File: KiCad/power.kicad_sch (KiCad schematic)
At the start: 30 parts, among them J1 Conn_01x03, J2 Conn_01x03, P1 USB_C_Plug_USB2.0, U1 TPS62056DGS, U2 TPS62056DGS, U3 LM66100DCK, U4 LM66100DCK

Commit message: changed components and excluded from BOM
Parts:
- J1, J2: now left out of the parts list
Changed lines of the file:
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@@
 		(body_style 1)
 		(exclude_from_sim no)
-		(in_bom yes)
+		(in_bom no)
 		(on_board yes)
 		(in_pos_files yes)
@@
 		(body_style 1)
 		(exclude_from_sim no)
-		(in_bom yes)
+		(in_bom no)
 		(on_board yes)
 		(in_pos_files yes)

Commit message: changed more part#
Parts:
- C3, C4, C9: JLCPCB Part C1590 -> C1591
- L1, L2: JLCPCB Part C1035 -> C86083
- R1, R2: JLCPCB Part C23186 -> C2907044
- R6, R8: JLCPCB Part C25803 -> C2906980
- R9: JLCPCB Part C25804 -> C2930027
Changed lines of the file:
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@@
 			)
 		)
-		(property "JLCPCB Part" "C23186"
+		(property "JLCPCB Part" "C2907044"
 			(at 46.99 179.07 0)
 			(hide yes)
@@
 			)
 		)
-		(property "JLCPCB Part" "C1035"
+		(property "JLCPCB Part" "C86083"
 			(at 63.5 107.95 90)
 			(hide yes)
@@
 			)
 		)
-		(property "JLCPCB Part" "C25803"
+		(property "JLCPCB Part" "C2906980"
 			(at 85.09 76.2 0)
 			(hide yes)
@@
 			)
 		)
-		(property "JLCPCB Part" "C25803"
+		(property "JLCPCB Part" "C2906980"
 			(at 85.09 121.92 0)
 			(hide yes)
@@
 			)
 		)
-		(property "JLCPCB Part" "C1590"
+		(property "JLCPCB Part" "C1591"
 			(at 62.23 121.92 0)
 			(hide yes)
@@
 			)
 		)
-		(property "JLCPCB Part" "C1590"
+		(property "JLCPCB Part" "C1591"
 			(at 184.15 49.53 0)
 			(hide yes)
@@
 			)
 		)
-		(property "JLCPCB Part" "C25804"
+		(property "JLCPCB Part" "C2930027"
 			(at 148.59 88.9 90)
 			(hide yes)
@@
 			)
 		)
-		(property "JLCPCB Part" "C1590"
+		(property "JLCPCB Part" "C1591"
 			(at 62.23 76.2 0)
 			(hide yes)
@@
 			)
 		)
-		(property "JLCPCB Part" "C23186"
+		(property "JLCPCB Part" "C2907044"
 			(at 58.42 179.07 0)
 			(hide yes)
@@
 			)
 		)
-		(property "JLCPCB Part" "C1035"
+		(property "JLCPCB Part" "C86083"
 			(at 63.5 62.23 90)
 			(hide yes)

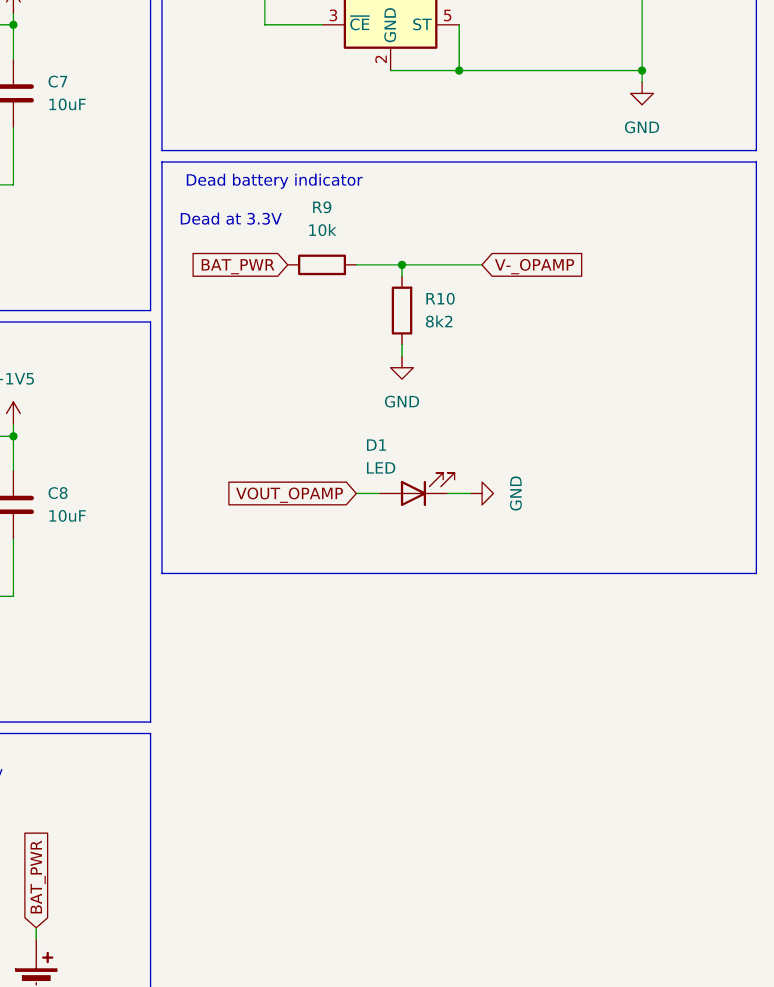
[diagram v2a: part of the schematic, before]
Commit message: changed some out of stock parts
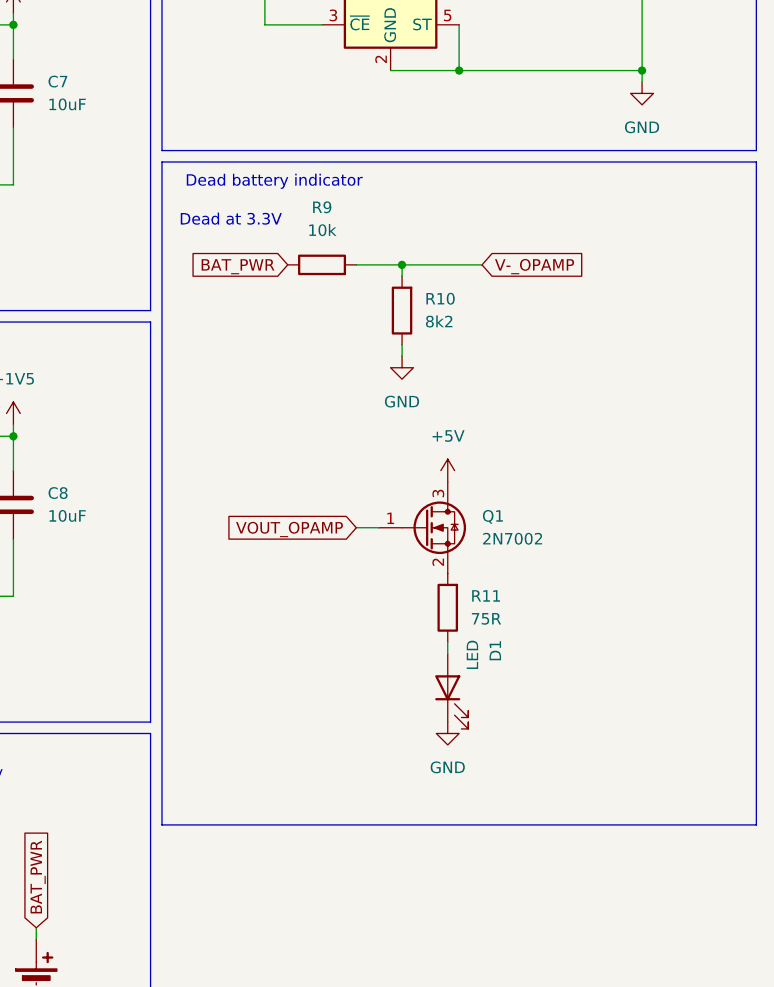
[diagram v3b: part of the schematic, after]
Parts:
- added Q1: 2N7002, Package_TO_SOT_SMD:SOT-23, symbol Transistor_FET:2N7002
- added R11: 75R, Resistor_SMD:R_0603_1608Metric_Pad0.98x0.95mm_HandSolder, symbol Device:R
- BT1: footprint AV-5:BatteryHolder_Keystone_2479_3xAAA -> footprints:BatteryHolder_Keystone_2479_3xAAA
- L1, L2: footprint Inductor_SMD:L_0603_1608Metric_Pad1.05x0.95mm_HandSolder -> Inductor_SMD:L_APV_APH0420; JLCPCB Part C86083 -> C181721
- R10: JLCPCB Part C25981 -> C114637
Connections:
- net +5V: now also Q1.3 (D)
- net VOUT_OPAMP: now also Q1.1 (G); no longer D1.2 (A)
- new net: D1.2 (A), R11.1
- new net: Q1.2 (S), R11.2
